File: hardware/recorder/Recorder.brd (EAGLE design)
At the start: 72.6 x 77.2 mm, 41 parts, among them U1 MCP4822-E/P, U2 LM6132BIN, U3 Value, U4 L7908CV, U5 L7808ABV, U6 ZVN4424A, U7 ZVN4424A, U8 DEV-16771_REDUCED_PINS

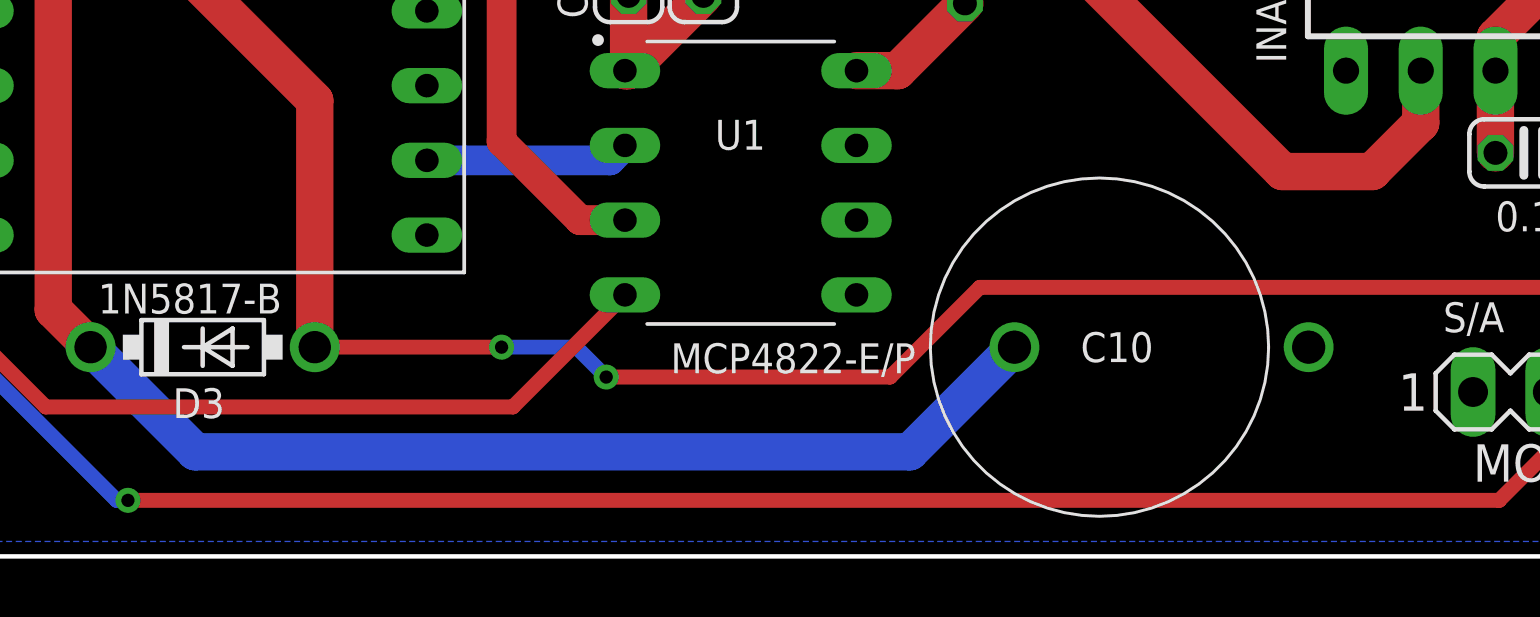
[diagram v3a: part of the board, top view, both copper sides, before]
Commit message: Move supercapacitor
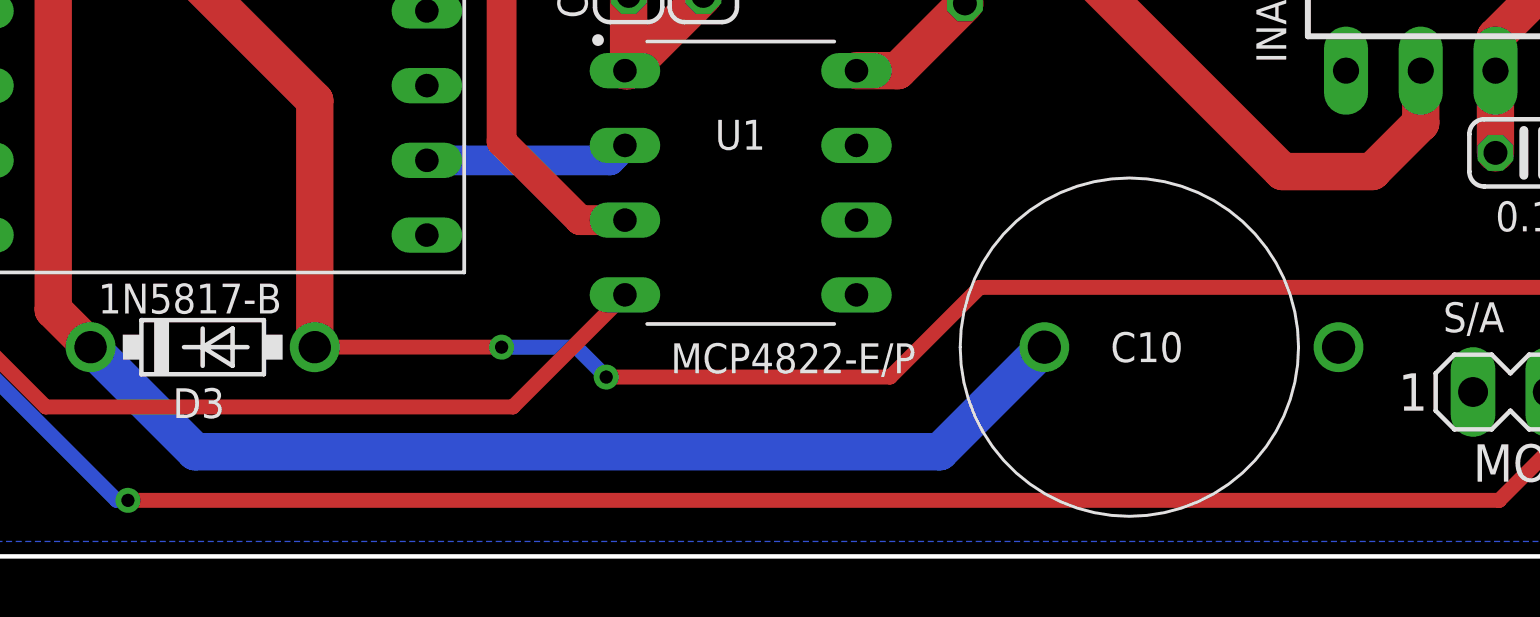
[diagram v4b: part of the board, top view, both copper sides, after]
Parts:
- moved C10 1.02 mm to (40.1, 7.11)
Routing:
- net N$2: track 51.4 -> 52.4 mm
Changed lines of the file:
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@@
 <drawing>
 <settings>
-<setting alwaysvectorfont="yes"/>
+<setting alwaysvectorfont="no"/>
 <setting verticaltext="up"/>
 </settings>
@@
 <attribute name="VALUE" x="53.594" y="2.667" size="1.27" layer="27" ratio="10"/>
 </element>
-<element name="C10" library="SamacSys_Parts" package="EDS224Z3R6H" value="EDS224Z3R6H" x="39.116" y="7.112" smashed="yes" rot="R180">
-<attribute name="DESCRIPTION" value="Supercapacitors / Ultracapacitors 0.22F 3.6V 85C" x="39.116" y="7.112" size="1.016" layer="27" rot="R180" display="off"/>
-<attribute name="HEIGHT" value="6mm" x="39.116" y="7.112" size="1.016" layer="27" rot="R180" display="off"/>
-<attribute name="MANUFACTURER_NAME" value="Cornell Dubilier" x="39.116" y="7.112" size="1.016" layer="27" rot="R180" display="off"/>
-<attribute name="MANUFACTURER_PART_NUMBER" value="EDS224Z3R6H" x="39.116" y="7.112" size="1.016" layer="27" rot="R180" display="off"/>
-<attribute name="MOUSER_PART_NUMBER" value="598-EDS224Z3R6H" x="39.116" y="7.112" size="1.016" layer="27" rot="R180" display="off"/>
-<attribute name="MOUSER_PRICE-STOCK" value="https://www.mouser.co.uk/ProductDetail/Cornell-Dubilier-CDE/EDS224Z3R6H?qs=bZr6mbWTK5lViRat0kLgfg%3D%3D" x="39.116" y="7.112" size="1.016" layer="27" rot="R180" display="off"/>
-<attribute name="NAME" x="42.762" y="7.112" size="1.016" layer="25" rot="R180" align="center"/>
+<element name="C10" library="SamacSys_Parts" package="EDS224Z3R6H" value="EDS224Z3R6H" x="40.132" y="7.112" smashed="yes" rot="R180">
+<attribute name="DESCRIPTION" value="Supercapacitors / Ultracapacitors 0.22F 3.6V 85C" x="40.132" y="7.112" size="1.016" layer="27" rot="R180" display="off"/>
+<attribute name="HEIGHT" value="6mm" x="40.132" y="7.112" size="1.016" layer="27" rot="R180" display="off"/>
+<attribute name="MANUFACTURER_NAME" value="Cornell Dubilier" x="40.132" y="7.112" size="1.016" layer="27" rot="R180" display="off"/>
+<attribute name="MANUFACTURER_PART_NUMBER" value="EDS224Z3R6H" x="40.132" y="7.112" size="1.016" layer="27" rot="R180" display="off"/>
+<attribute name="MOUSER_PART_NUMBER" value="598-EDS224Z3R6H" x="40.132" y="7.112" size="1.016" layer="27" rot="R180" display="off"/>
+<attribute name="MOUSER_PRICE-STOCK" value="https://www.mouser.co.uk/ProductDetail/Cornell-Dubilier-CDE/EDS224Z3R6H?qs=bZr6mbWTK5lViRat0kLgfg%3D%3D" x="40.132" y="7.112" size="1.016" layer="27" rot="R180" display="off"/>
+<attribute name="NAME" x="43.778" y="7.112" size="1.016" layer="25" rot="R180" align="center"/>
 </element>
 <element name="R_GAIN_100" library="rcl" library_urn="urn:adsk.eagle:library:334" package="0207/10" package3d_urn="urn:adsk.eagle:package:23491/2" value="511R" x="65.532" y="21.336" smashed="yes" rot="R90">
@@
 <contactref element="C10" pad="1"/>
 <wire x1="7.874" y1="7.112" x2="11.43" y2="3.556" width="1.27" layer="16"/>
-<wire x1="35.72" y1="3.556" x2="39.276" y2="7.112" width="1.27" layer="16"/>
-<wire x1="11.43" y1="3.556" x2="35.72" y2="3.556" width="1.27" layer="16"/>
+<wire x1="36.736" y1="3.556" x2="40.292" y2="7.112" width="1.27" layer="16"/>
+<wire x1="11.43" y1="3.556" x2="36.736" y2="3.556" width="1.27" layer="16"/>
 </signal>
 <signal name="N$7">

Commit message: Add minor changes to the hardware
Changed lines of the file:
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@@
 <via x="51.816" y="50.8" extent="1-16" drill="1"/>
 <wire x1="51.816" y1="50.8" x2="44.704" y2="50.8" width="1.27" layer="16"/>
-<wire x1="44.704" y1="50.8" x2="41.148" y2="47.244" width="1.27" layer="16"/>
-<via x="41.148" y="47.244" extent="1-16" drill="1"/>
-<wire x1="41.148" y1="47.244" x2="38.862" y2="44.958" width="1.27" layer="1"/>
+<wire x1="44.704" y1="50.8" x2="40.894" y2="46.99" width="1.27" layer="16"/>
+<via x="40.894" y="46.99" extent="1-16" drill="1"/>
+<wire x1="40.894" y1="46.99" x2="38.862" y2="44.958" width="1.27" layer="1"/>
 <wire x1="38.862" y1="44.958" x2="36.99" y2="44.958" width="1.27" layer="1"/>
 <wire x1="49.276" y1="27.94" x2="50.8" y2="27.94" width="1.27" layer="1"/>
@@
 <wire x1="34.798" y1="61.715" x2="34.847" y2="61.666" width="1.27" layer="1"/>
 <wire x1="34.847" y1="61.666" x2="34.847" y2="58.625" width="1.27" layer="1"/>
-<wire x1="43.18" y1="43.18" x2="44.196" y2="42.164" width="1.27" layer="1"/>
+<wire x1="42.926" y1="43.434" x2="44.196" y2="42.164" width="1.27" layer="1"/>
 <wire x1="44.196" y1="42.164" x2="45.72" y2="42.164" width="1.27" layer="1"/>
-<wire x1="34.847" y1="58.625" x2="43.18" y2="50.292" width="1.27" layer="1"/>
-<wire x1="43.18" y1="50.292" x2="43.18" y2="43.18" width="1.27" layer="1"/>
+<wire x1="34.847" y1="58.625" x2="42.926" y2="50.546" width="1.27" layer="1"/>
+<wire x1="42.926" y1="50.546" x2="42.926" y2="43.434" width="1.27" layer="1"/>
 <contactref element="C13" pad="2"/>
 <wire x1="41.275" y1="42.164" x2="45.72" y2="42.164" width="1.27" layer="1"/>

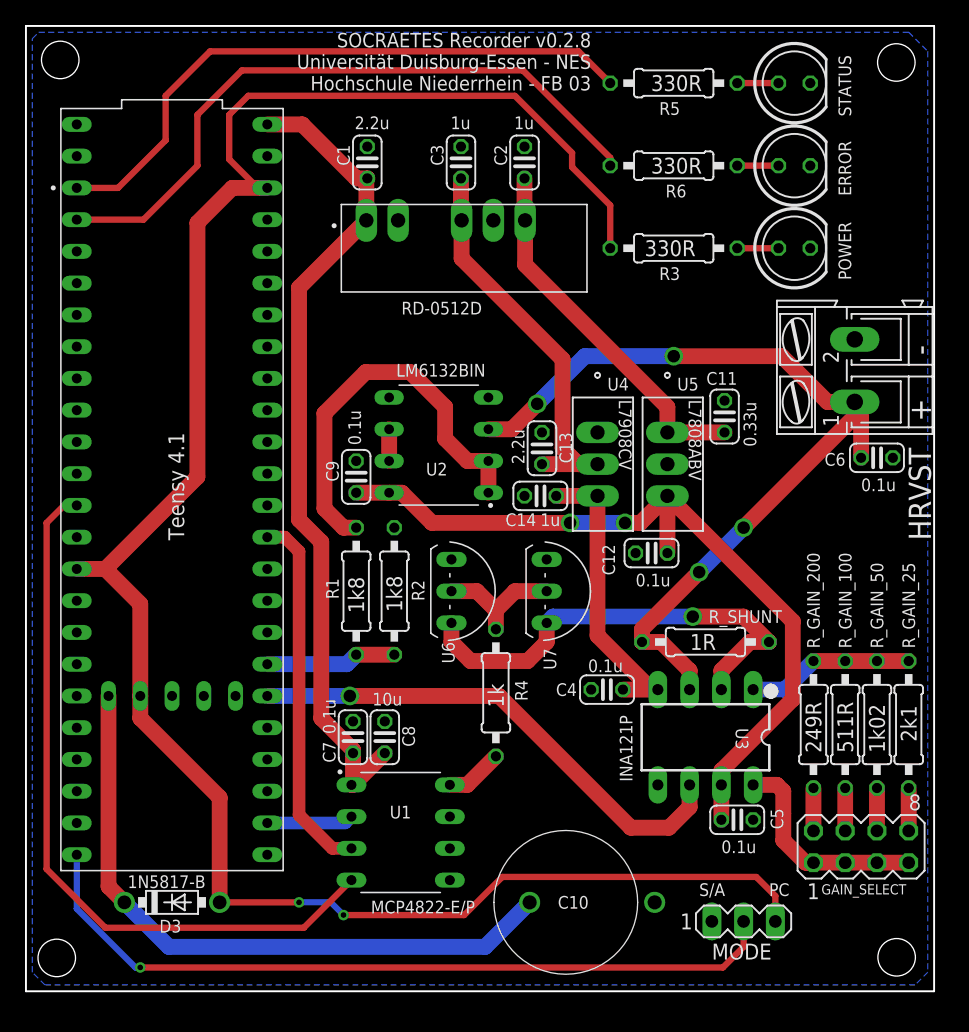
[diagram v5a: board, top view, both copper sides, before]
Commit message: Update part designators
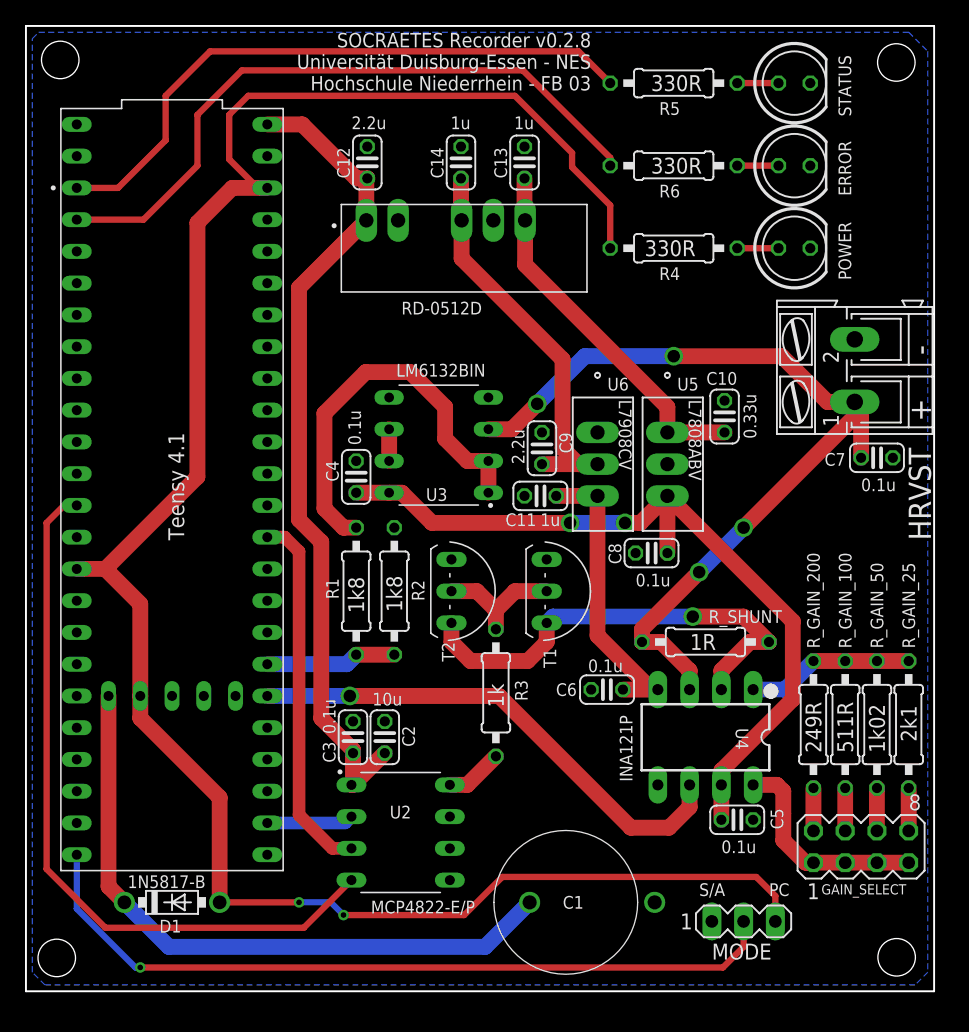
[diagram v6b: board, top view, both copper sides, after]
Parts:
- removed U8: DEV-16771_REDUCED_PINS, DEV-16771 (Teensy 41):MODULE_DEV-16771_REDUCED_PINS
- added T2: ZVN4424A, NES_Solar_Cell_Recorder_And_Emulator:TO92-CBE
- C1: value 2.2u -> EDS224Z3R6H; device rcl:C025-024X044 -> SamacSys_Parts:EDS224Z3R6H
- C10: value EDS224Z3R6H -> 0.33u; device SamacSys_Parts:EDS224Z3R6H -> rcl:C025-024X044
- C11: value 0.33u -> 1u
- C12, C9: value 0.1u -> 2.2u
- C13: value 2.2u -> 1u
- C2: value 1u -> 10u
- C3: value 1u -> 0.1u
- C8: value 10u -> 0.1u
- R3: value 330R -> 1k
- R4: value 1k -> 330R
- U1: value MCP4822-E/P -> DEV-16771_REDUCED_PINS; device MCP4822-E_P:DIP787W46P254L927H533Q8 -> DEV-16771 (Teensy 41):MODULE_DEV-16771_REDUCED_PINS
- U2: value LM6132BIN -> MCP4822-E/P; device LM6132BIN:DIP794W45P254L959H508Q8 -> MCP4822-E_P:DIP787W46P254L927H533Q8
- U3: value Value -> LM6132BIN; device INA121PA:P0008A -> LM6132BIN:DIP794W45P254L959H508Q8
- U4: value L7908CV -> Value; device L7908CV:TO-220_STM -> INA121PA:P0008A
- U6: value ZVN4424A -> L7908CV; device NES_Solar_Cell_Recorder_And_Emulator:TO92-CBE -> L7908CV:TO-220_STM
- moved C1 60.6 mm to (40.1, 7.11), turned to 180 degrees
- moved C7 47.5 mm to (68.1, 42.7), turned to 0 degrees
- moved C2 47.3 mm to (28.7, 20.3)
- moved C3 46.8 mm to (26.2, 20.3)
- moved C10 41.9 mm to (55.9, 46.0), turned to 90 degrees
- moved C12 38.6 mm to (27.3, 66.3), turned to 90 degrees
- moved R3 38.3 mm to (37.6, 23.9), turned to 270 degrees
- moved R4 38.3 mm to (51.8, 59.4), turned to 180 degrees
- moved U1 33.0 mm to (11.7, 40.1), turned to 270 degrees
- moved U3 31.6 mm to (33.0, 43.7), turned to 180 degrees
- moved U2 31.1 mm to (30.0, 12.7), turned to 0 degrees
- moved C6 28.5 mm to (46.5, 24.1), turned to 180 degrees
- moved C14 27.4 mm to (34.8, 66.3), turned to 90 degrees
- moved C4 26.3 mm to (26.4, 41.1), turned to 90 degrees
- moved C8 25.9 mm to (50.0, 35.1), turned to 0 degrees
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- renumbered D3 to D1, U7 to T1
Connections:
- net +12V: now also C10.1, C13.1; no longer C11.1, C2.1
- net +3V3: now also R4.2, U1.3.3V_1, U1.3.3V_2, U1.3.3V_3; no longer R3.2, U8.3.3V_1, U8.3.3V_2, U8.3.3V_3
- net +5V: now also C12.1, C2.1, C3.1, U1.VIN, U2.1; no longer C1.1, C7.1, C8.1, U1.1, U8.VIN
- net +8V: now also C4.1, C8.2, U3.8, U4.7; no longer C12.2, C9.1, U2.8, U3.7
- net -12V: now also C14.1, C9.2, U6.2; no longer C13.2, C3.1, U4.2
- net -8V: now also C11.2, C6.1, U4.4, U6.3; no longer C14.2, C4.1, U3.4, U4.3
- net CURRENT_SENSE_AMP_OUTPUT: now also U1.38, U4.6; no longer U3.6, U8.38
- net DAC_CS: now also U1.34, U2.2; no longer U1.2, U8.34
- net DAC_MOSI: now also U1.11, U2.4; no longer U1.4, U8.11
- net DAC_SCK: now also U1.13, U2.3; no longer U1.3, U8.13
- net ERROR_LED: now also U1.2; no longer U8.2
- net GND: now also C11.1, C12.2, C13.2, C14.2, C8.1, C9.1, T2.SOURCE, U1.GND1, U1.GND2, U1.GND3, U1.GND4, U2.7, U3.4, U4.5, U6.1; no longer C11.2, C12.1, C13.1, C14.1, C8.2, C9.2, U1.5, U1.7, U2.4, U4.1, U6.SOURCE, U8.GND1, U8.GND2, U8.GND3, U8.GND4
- net HARVESTER+: now also C7.1, U4.3; no longer C6.1, U2.3
- net HARVESTER_VOLTAGE_DIVIDER_OUTPUT: now also U1.39; no longer U8.39
- net JUMPER_SELECT_MODE: now also U1.32; no longer U8.32
- net MOSFET_DAC_OUTPUT: now also R3.2, U2.8; no longer R4.2, U1.8
- net N$11: now also R3.1, T2.GATE; no longer R4.1, U6.GATE
- net N$12: now also U4.1; no longer U3.1
- net N$13: now also U4.8; no longer U3.8
- net N$2: now also C1.1, U1.VBAT; no longer C10.1, U8.VBAT
- net N$5: now also U3.6, U3.7; no longer U2.6, U2.7
- net N$6: now also T2.DRAIN, U4.2; no longer U3.2, U6.DRAIN
- net N$8: now also U3.1, U3.2; no longer U2.1, U2.2
- net N$9: now also R4.1; no longer R3.1
- net STATUS_LED: now also U1.1; no longer U8.1

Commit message: Add new recorder MOSFET and update the existing one
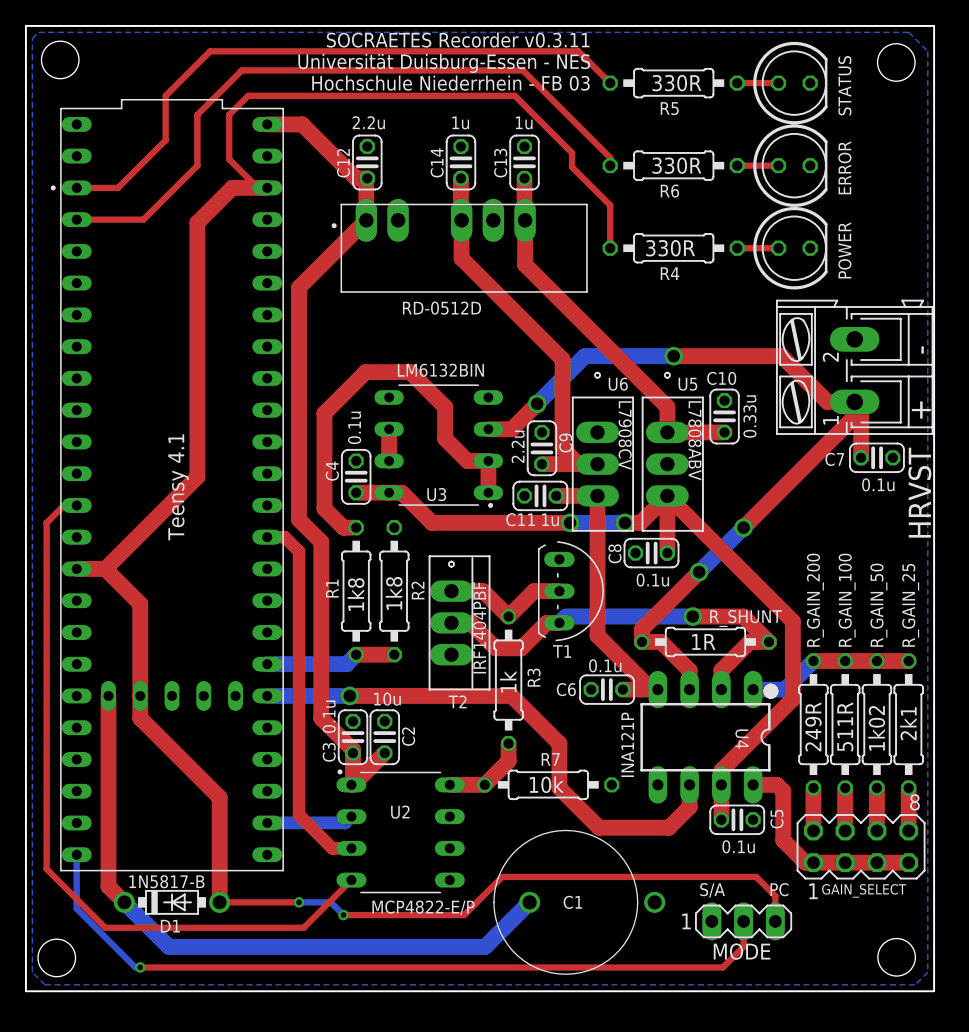
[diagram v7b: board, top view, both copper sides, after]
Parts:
- added R7: 10k, rcl:0207/10
- T1: value ZVN4424A -> VN0109N3-G-ND
- T2: value ZVN4424A -> IRF1404PBF; device NES_Solar_Cell_Recorder_And_Emulator:TO92-CBE -> IRF1404PBF:PG-TO220-3-904_INF
- moved R3 1.44 mm to (38.6, 24.9)
- moved T1 1.02 mm to (42.7, 32.0)
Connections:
- net GND: now also R7.1, T2.S; no longer T2.SOURCE
- net MOSFET_DAC_OUTPUT: now also R7.2
- net N$11: now also T2.G; no longer T2.GATE
- net N$6: now also T2.D; no longer T2.DRAIN
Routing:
- net N$6: track 37.0 -> 34.4 mm
- net MOSFET_DAC_OUTPUT: track 4.63 -> 6.89 mm
- net CURRENT_SENSE_AMP_OUTPUT: track 40.6 -> 42.7 mm
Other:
- board text added: "SOCRAETES Recorder v0.3.11 Universität Duisburg-Essen - NES Hochschule Niederrhein - FB 03"
- board text removed: "SOCRAETES Recorder v0.2.8 Universität Duisburg-Essen - NES Hochschule Niederrhein - FB 03"
